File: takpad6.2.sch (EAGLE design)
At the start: 75 parts, among them J1 SD_CARD_SOCKET, J10 AUDIO_JACK_TRRSSMD_RA, J3 AVR_SPI_PROG_3X2PTH, T1 0, T3 0, U1 ATMEGA328P_TQFP, U4 LM386N, Y1 20MHz

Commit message: Add files via upload
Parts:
- removed C22, C24: 1uF, SparkFun-Capacitors:47PF-0603-50V-5%
- added C17, C21: 1uF, SparkFun-Capacitors:47PF-0603-50V-5%
- added TP10, TP11, TP12, TP13, TP14, TP15, TP5, TP6, TP7, TP8, TP9: TPPAD1-17, testpad:TPPAD1-17
- added TP16, TP17: TPB1,27, testpad:TPB1,27
- TP1, TP4: value TPPAD1-17 -> TPB1,27; device testpad:TPPAD1-17 -> testpad:TPB1,27
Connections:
- removed net N$2: C23.2, U1.VCC@4
- removed net N$3: C22.2, U1.AVCC
- removed net N$4: C24.2, U1.VCC@6
- net BAT: now also TP1.TP
- net GND: now also C17.1, C21.1, C23.1
- net PB6: now also TP13.TP
- net PB7: now also TP14.TP
- net RST: now also TP15.TP
- net SENS1LED: now also TP9.TP
- net SENS2LED: now also TP10.TP
- net SENS3LED: now also TP11.TP
- net SENS4LED: now also TP12.TP
- net SENSOR1OUT: now also TP8.TP
- net SENSOR2OUT: now also TP7.TP
- net SENSOR3OUT: now also TP6.TP
- net SENSOR4OUT: now also TP5.TP
- net TEMPSENSE: now also TP17.TP
- net V+: now also C17.2, C21.2, C23.2, U1.AVCC, U1.VCC@4, U1.VCC@6; no longer C22.1, C23.1, C24.1, TP1.TP
- net VIN: now also TP16.TP
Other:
- moved on the sheet: C15, C23

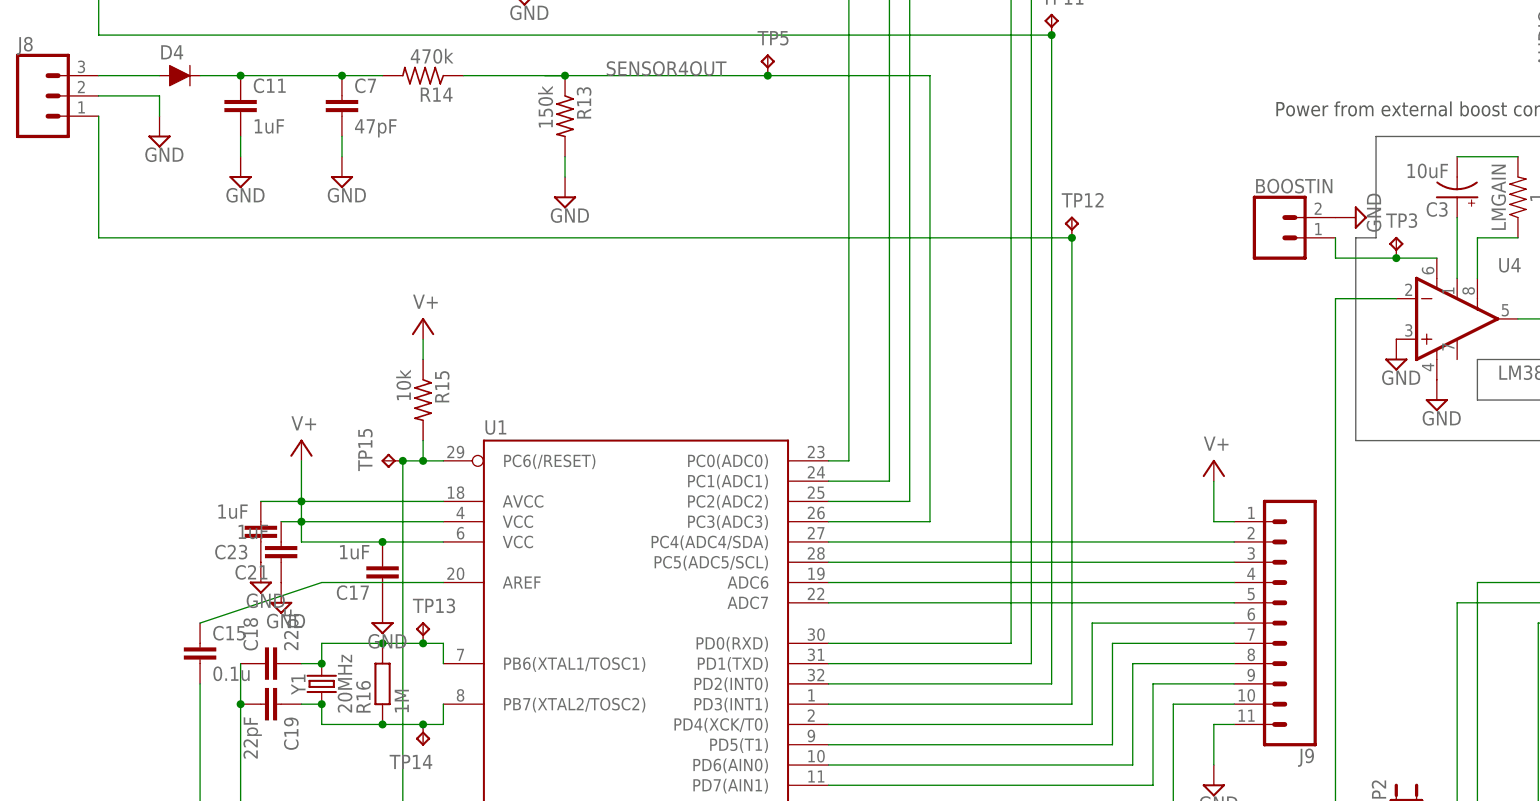
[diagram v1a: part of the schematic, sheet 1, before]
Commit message: Add files via upload
TO DO LIST:

MAJOR - 0.1uF caps by voltage pins - done (some of these are 1uF, is this the right value?)

Label pinouts, (not really sure what I am supposed to label)

change a few font sizes

some routing

some TP placement
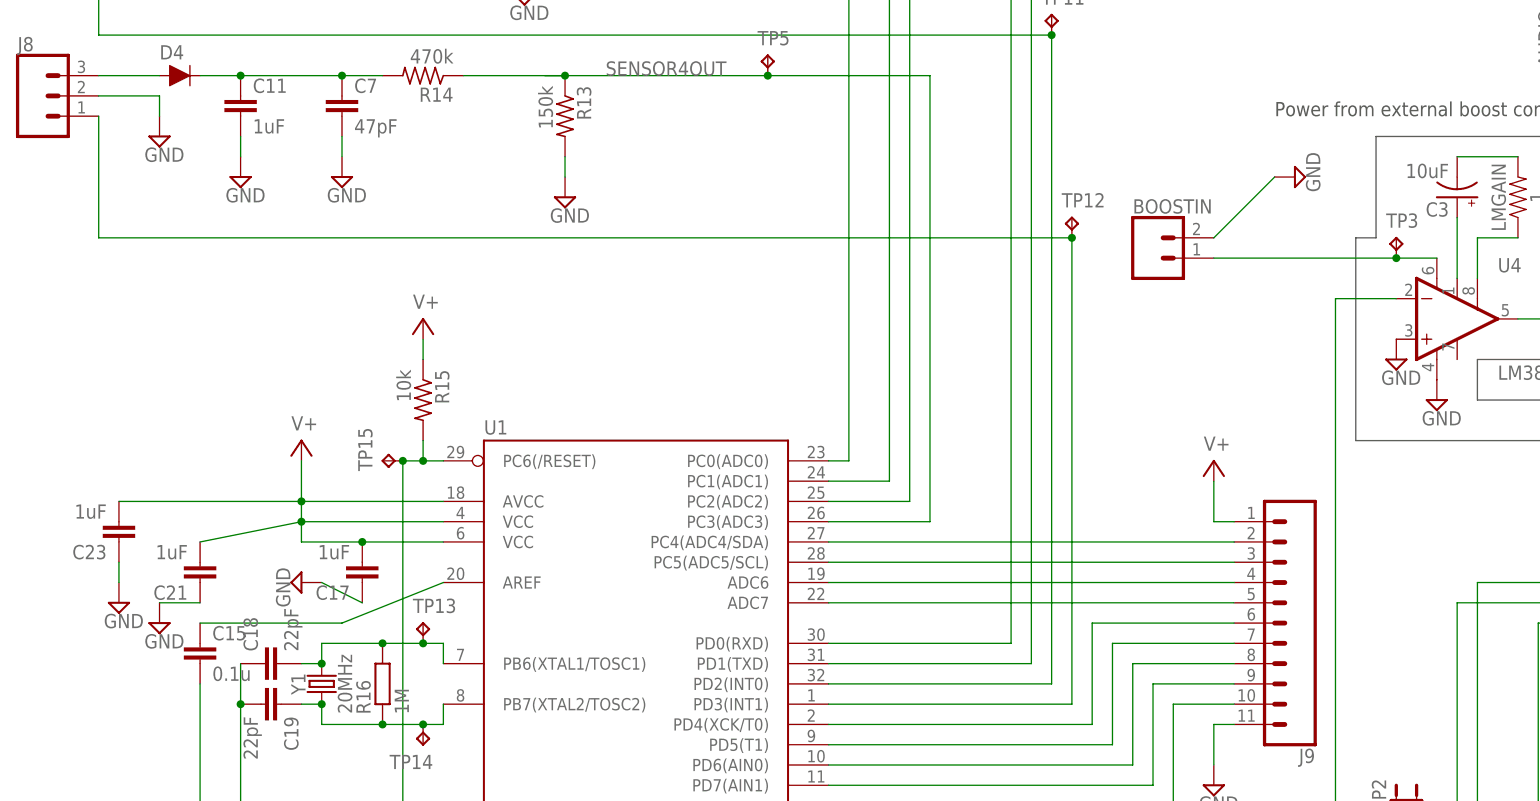
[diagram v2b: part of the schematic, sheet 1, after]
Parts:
- TP10, TP11, TP12, TP13, TP14, TP15, TP2, TP3, TP5, TP6, TP7, TP8, TP9: value TPPAD1-17 -> TPB1,27; device testpad:TPPAD1-17 -> testpad:TPB1,27
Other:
- moved on the sheet: BOOSTIN, C17, C21, C23

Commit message: Add files via upload
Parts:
- added C22: 10uF, SparkFun-Capacitors:10UF-POLAR-RADIAL-2.5MM-KIT-25V-20%
- added C24: 0.1uF, SparkFun-Capacitors:10UF-POLAR-RADIAL-2.5MM-KIT-25V-20%
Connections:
- new net BYPASS: C24.+, U4.BP
- net GND: now also C22.-, C24.-
- net UPCONVERTERINPUT: now also C22.+
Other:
- note added: "Unused"
- moved on the sheet: C21, C23

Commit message: Add files via upload
nearly done hope this works, cross fingers
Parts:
- added T2: 0, SparkFun-Resistors:1KOHM-HORIZ-1/4W-1%
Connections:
- net SENSOR1IN: now also T2.2
- net SENSOR1OUT: now also T2.1
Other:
- moved on the sheet: C17, C21, C23, R8, T3
